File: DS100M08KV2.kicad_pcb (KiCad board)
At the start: 4 copper layers, 100 x 52 mm, 129 parts, among them J1 wire2board, J10 BNC_panel_mount, J11 wire2board, J2 Conn_01x04_Socket, J3 wire2board, J4 wire2board, J5 USB_C_floating, J8 red_safety_4mm_connector, J9 black_safety_4mm_connector, Q1 BD679, Q3 CMSN3416K-HF, Q4 BD680, Q5 CMSN3416K-HF, SW1 SW_DPDT_x2, SW2 SW_DPDT_x2, U1 AD8066, U2 AP9101CK6, U4 AD8009, U6 BQ21040DBV, U7 TLV61070ADBVR

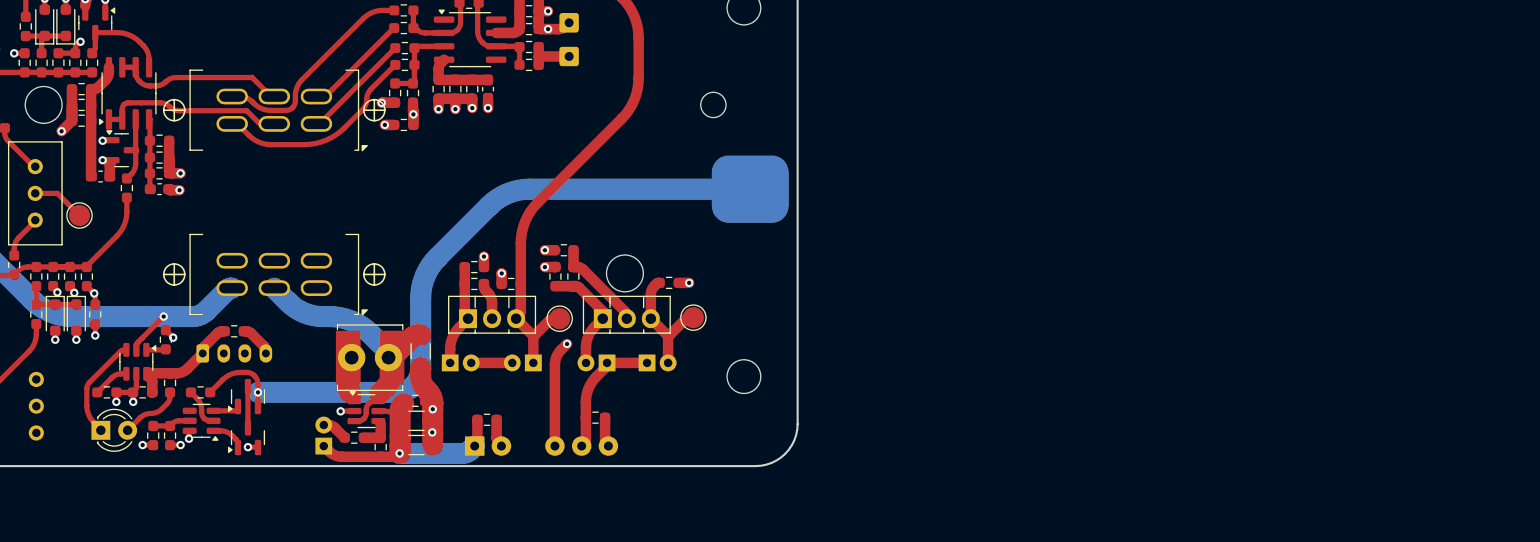
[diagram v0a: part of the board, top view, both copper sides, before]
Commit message: New sims, added switcher to PCB.
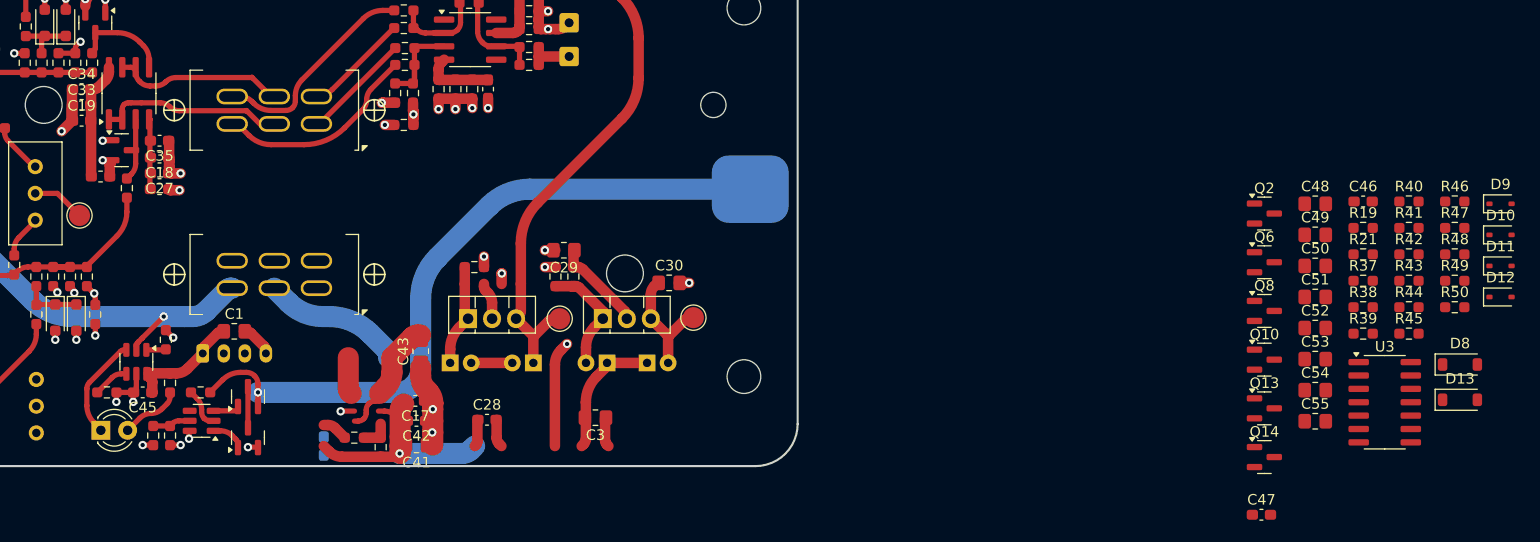
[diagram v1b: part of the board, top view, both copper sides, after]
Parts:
- removed C31: 1u, Resistor_SMD:R_0603_1608Metric_Pad0.98x0.95mm_HandSolder
- removed L2: 4.7u, Inductor_THT:L_Radial_D7.5mm_P3.50mm_Fastron_07P
- removed L3: 4.7u, Inductor_SMD:L_Bourns_SRN6045TA
- removed PS1: IA0509S, Converter_DCDC:Converter_DCDC_XP_POWER-IAxxxxS_THT
- removed R31: 1k, Resistor_SMD:R_0603_1608Metric_Pad0.98x0.95mm_HandSolder
- removed U7: TLV61070ADBVR, Package_TO_SOT_SMD:SOT-23-6
- added C46: 1u, Capacitor_SMD:C_0603_1608Metric_Pad1.08x0.95mm_HandSolder, F.Cu at (253.7, 126.9)
- added C47: 100n, Capacitor_SMD:C_0603_1608Metric_Pad1.08x0.95mm_HandSolder, F.Cu at (244.0, 156.6)
- added C48: 10u, Resistor_SMD:R_0805_2012Metric_Pad1.20x1.40mm_HandSolder, F.Cu at (249.2, 127.1)
- added C49: 10u, Resistor_SMD:R_0805_2012Metric_Pad1.20x1.40mm_HandSolder, F.Cu at (249.2, 130.0)
- added C50: 10u, Resistor_SMD:R_0805_2012Metric_Pad1.20x1.40mm_HandSolder, F.Cu at (249.2, 133.0)
- added C51: 10u, Resistor_SMD:R_0805_2012Metric_Pad1.20x1.40mm_HandSolder, F.Cu at (249.2, 135.9)
- added C52: 10u, Resistor_SMD:R_0805_2012Metric_Pad1.20x1.40mm_HandSolder, F.Cu at (249.2, 138.9)
- added C53: 10u, Resistor_SMD:R_0805_2012Metric_Pad1.20x1.40mm_HandSolder, F.Cu at (249.2, 141.8)
- added C54: 10u, Resistor_SMD:R_0805_2012Metric_Pad1.20x1.40mm_HandSolder, F.Cu at (249.2, 144.8)
- added C55: 10u, Resistor_SMD:R_0805_2012Metric_Pad1.20x1.40mm_HandSolder, F.Cu at (249.2, 147.7)
- added D10: 1N4148WS, Diode_SMD:D_SOD-323, F.Cu at (266.8, 130.0)
- added D11: 1N4148WS, Diode_SMD:D_SOD-323, F.Cu at (266.8, 133.0)
- added D12: 1N4148WS, Diode_SMD:D_SOD-323, F.Cu at (266.8, 135.9)
- added D13: 1N4148W, Diode_SMD:D_SOD-123, F.Cu at (262.9, 145.7)
- added D8: 1N4148W, Diode_SMD:D_SOD-123, F.Cu at (262.9, 142.3)
- added D9: 1N4148WS, Diode_SMD:D_SOD-323, F.Cu at (266.8, 127.1)
- added Q10: AO3401A, Package_TO_SOT_SMD:SOT-23, F.Cu at (244.3, 141.9)
- added Q13: AO3400A, Package_TO_SOT_SMD:SOT-23, F.Cu at (244.3, 146.5)
- added Q14: AO3400A, Package_TO_SOT_SMD:SOT-23, F.Cu at (244.3, 151.1)
- added Q2: MMBT5551L, Package_TO_SOT_SMD:SOT-23, F.Cu at (244.3, 128.0)
- added Q6: MMBT5551L, Package_TO_SOT_SMD:SOT-23, F.Cu at (244.3, 132.6)
- added Q8: AO3401A, Package_TO_SOT_SMD:SOT-23, F.Cu at (244.3, 137.3)
- added R19: 39k, Resistor_SMD:R_0603_1608Metric_Pad0.98x0.95mm_HandSolder, F.Cu at (253.7, 129.4)
- added R21: 470k, Resistor_SMD:R_0603_1608Metric_Pad0.98x0.95mm_HandSolder, F.Cu at (253.7, 131.9)
- added R37: 100k, Resistor_SMD:R_0603_1608Metric_Pad0.98x0.95mm_HandSolder, F.Cu at (253.7, 134.4)
- added R38: 100k, Resistor_SMD:R_0603_1608Metric_Pad0.98x0.95mm_HandSolder, F.Cu at (253.7, 136.9)
- added R39: 470k, Resistor_SMD:R_0603_1608Metric_Pad0.98x0.95mm_HandSolder, F.Cu at (253.7, 139.4)
- added R40: 10k, Resistor_SMD:R_0603_1608Metric_Pad0.98x0.95mm_HandSolder, F.Cu at (258.1, 126.9)
- added R41: 470k, Resistor_SMD:R_0603_1608Metric_Pad0.98x0.95mm_HandSolder, F.Cu at (258.1, 129.4)
- added R42: 1k, Resistor_SMD:R_0603_1608Metric_Pad0.98x0.95mm_HandSolder, F.Cu at (258.1, 131.9)
- added R43: 470k, Resistor_SMD:R_0603_1608Metric_Pad0.98x0.95mm_HandSolder, F.Cu at (258.1, 134.4)
- added R44: 470k, Resistor_SMD:R_0603_1608Metric_Pad0.98x0.95mm_HandSolder, F.Cu at (258.1, 136.9)
- added R45: 1Meg, Resistor_SMD:R_0603_1608Metric_Pad0.98x0.95mm_HandSolder, F.Cu at (258.1, 139.4)
- added R46: 1Meg, Resistor_SMD:R_0603_1608Metric_Pad0.98x0.95mm_HandSolder, F.Cu at (262.4, 126.9)
- added R47: 470k, Resistor_SMD:R_0603_1608Metric_Pad0.98x0.95mm_HandSolder, F.Cu at (262.4, 129.4)
- added R48: 1Meg, Resistor_SMD:R_0603_1608Metric_Pad0.98x0.95mm_HandSolder, F.Cu at (262.4, 131.9)
- added R49: 1Meg, Resistor_SMD:R_0603_1608Metric_Pad0.98x0.95mm_HandSolder, F.Cu at (262.4, 134.4)
- added R50: 1k, Resistor_SMD:R_0603_1608Metric_Pad0.98x0.95mm_HandSolder, F.Cu at (262.4, 136.9)
- added U3: 74HC14D653, Package_SO:SOIC-14_3.9x8.7mm_P1.27mm, F.Cu at (255.8, 145.9)
- C1, C29, C3, C30: value 1u -> 10u; footprint Resistor_SMD:R_0603_1608Metric_Pad0.98x0.95mm_HandSolder -> Resistor_SMD:R_0805_2012Metric_Pad1.20x1.40mm_HandSolder
- C17: value 1u -> 1n; footprint Resistor_SMD:R_0603_1608Metric_Pad0.98x0.95mm_HandSolder -> Capacitor_SMD:C_0603_1608Metric_Pad1.08x0.95mm_HandSolder
- C18: value 100n -> 10u; footprint Resistor_SMD:R_0603_1608Metric_Pad0.98x0.95mm_HandSolder -> Capacitor_SMD:C_0603_1608Metric_Pad1.08x0.95mm_HandSolder
- C19: value 1u -> 10u; footprint Resistor_SMD:R_0603_1608Metric_Pad0.98x0.95mm_HandSolder -> Capacitor_SMD:C_0603_1608Metric_Pad1.08x0.95mm_HandSolder
- C23, C24: value 470p -> 1n
- C27, C28: value 1u -> 100n; footprint Resistor_SMD:R_0603_1608Metric_Pad0.98x0.95mm_HandSolder -> Capacitor_SMD:C_0603_1608Metric_Pad1.08x0.95mm_HandSolder
- C33: value 100n -> 100p; footprint Resistor_SMD:R_0603_1608Metric_Pad0.98x0.95mm_HandSolder -> Capacitor_SMD:C_0603_1608Metric_Pad1.08x0.95mm_HandSolder
- C34: value 1n -> 100p; footprint Resistor_SMD:R_0603_1608Metric_Pad0.98x0.95mm_HandSolder -> Capacitor_SMD:C_0603_1608Metric_Pad1.08x0.95mm_HandSolder
- C35: value 1n -> 100n; footprint Resistor_SMD:R_0603_1608Metric_Pad0.98x0.95mm_HandSolder -> Capacitor_SMD:C_0603_1608Metric_Pad1.08x0.95mm_HandSolder
- C40: value 47u -> 1u; footprint Capacitor_THT:CP_Radial_D5.0mm_P2.00mm -> Capacitor_SMD:C_0603_1608Metric_Pad1.08x0.95mm_HandSolder
- C41, C43: footprint Resistor_SMD:R_1206_3216Metric_Pad1.30x1.75mm_HandSolder -> Resistor_SMD:R_0805_2012Metric_Pad1.20x1.40mm_HandSolder
- C42: value 10u -> 100n; footprint Resistor_SMD:R_1206_3216Metric_Pad1.30x1.75mm_HandSolder -> Capacitor_SMD:C_0603_1608Metric_Pad1.08x0.95mm_HandSolder
- C45: footprint Resistor_SMD:R_0603_1608Metric_Pad0.98x0.95mm_HandSolder -> Capacitor_SMD:C_0603_1608Metric_Pad1.08x0.95mm_HandSolder
- Q1: value BD679 -> MMBT5401
- Q4: value BD680 -> MMBT5401
- R12, R5: value 10k -> 5k
- R27: value 10k -> 22k
- R28: value 91k -> 100k
- R32: value 2k2 -> 22k
- R34: value 2k2 -> 100k
- U1: value AD8066 -> RS8752XK
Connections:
- BT1 pad 1: +BAT -> +BATT
- BT1 pad 2: -BAT -> -BATT
- C1 pad 1: +VBUS -> -BATT
- C1 pad 2: Earth -> -VIN
- C16 pad 1: Net-(Q1-B) -> Net-(Q2-B)
- C17 pad 1: Earth -> -BATT
- C17 pad 2: +5V_BOOST -> Net-(C17-Pad2)
- C18 pad 1: 0 -> Net-(U1C-V-)
- C18 pad 2: Net-(U1C-V-) -> 0
- C19 pad 1: 0 -> Net-(U1C-V+)
- C19 pad 2: Net-(U1C-V+) -> 0
- C20 pad 2: Net-(Q4-B) -> Net-(Q1-B)
- C27 pad 1: 0 -> PMOS_GATE
- C27 pad 2: Net-(U1C-V-) -> Net-(D8-A)
- C28 pad 1: +5V_BOOST -> Earth
- C28 pad 2: Earth -> +VBUS
- C29 pad 1: Net-(PS1--Vout) -> 0
- C29 pad 2: 0 -> +2V5
- C3 pad 1: Net-(PS1-+Vout) -> -VIN
- C30 pad 1: -5V -> -2V5
- C33 pad 1: 0 -> -BATT
- C33 pad 2: Net-(U1C-V+) -> Net-(D11-K)
- C34 pad 1: 0 -> -BATT
- C34 pad 2: Net-(U1C-V+) -> Net-(D12-A)
- C36 pad 2: -5V -> -2V5
- C40 pad 1: +5V_BOOST -> Earth
- C40 pad 2: Earth -> +VBUS
- C41 pad 1: Earth -> Net-(Q13-D)
- C41 pad 2: +5V_BOOST -> Net-(Q10-D)
- C42 pad 1: Earth -> NMOS_GATE
- C42 pad 2: +5V_BOOST -> Net-(D13-A)
- C43 pad 1: Earth -> Net-(Q13-D)
- C43 pad 2: Net-(SW2A-B) -> Net-(Q10-D)
- C44 pad 1: +5V -> +2V5
- C45 pad 1: +VBUS -> -BATT
- C45 pad 2: Earth -> +VIN
- Q1 pad 2: Net-(PS1-+Vout) -> -2V5
- Q1 pad 3: +5V -> -VIN
- Q4 pad 2: Net-(PS1--Vout) -> 0
- Q4 pad 3: -5V -> Net-(Q1-B)
- R27 pad 1: Earth -> Net-(Q6-B)
- R27 pad 2: Net-(U7-FB) -> 0
- R28 pad 1: Net-(U7-FB) -> Net-(Q1-B)
- R28 pad 2: +5V_BOOST -> Net-(Q4-B)
- R32 pad 1: 0 -> Net-(Q4-B)
- R32 pad 2: Net-(Q1-B) -> 0
- R33 pad 1: Net-(Q4-B) -> Net-(Q2-B)
- R33 pad 2: Net-(PS1--Vout) -> +VIN
- R34 pad 1: 0 -> Net-(Q6-B)
- R34 pad 2: Net-(Q4-B) -> Net-(Q2-B)
- SW2 pad 2: Net-(SW2A-B) -> +VIN
- SW2 pad 3: +BAT -> +BATT
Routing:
- net Net-(PS1-+Vout): track 24.7 -> 0.00 mm
- net Net-(SW2A-B): track 24.2 -> 0.00 mm
- net -2V5: track 0.00 -> 21.9 mm
- net +VIN: track 0.00 -> 13.4 mm, vias 0 -> 1
- net Net-(Q10-D): track 0.00 -> 10.8 mm
- net (no net): track 0.00 -> 6.38 mm
- net Net-(U7-SW): track 3.49 -> 0.00 mm
- net Net-(Q6-B): track 0.00 -> 3.44 mm, vias 0 -> 1
- net 0: track 67.2 -> 64.2 mm, vias 24 -> 21
- net Net-(U7-FB): track 2.89 -> 0.00 mm
- net -VIN: track 0.00 -> 2.80 mm
- net +VBUS: track 10.9 -> 13.6 mm
- net +5V_BOOST: track 24.8 -> 22.2 mm, vias 1 -> 0
- net Earth: track 26.3 -> 23.8 mm
- net Net-(Q4-B): track 11.5 -> 12.5 mm, vias 0 -> 2
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
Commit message: Sims, schem.
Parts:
- removed FB3, FB4: FerriteBead, Inductor_SMD:L_0603_1608Metric_Pad1.05x0.95mm_HandSolder
- removed RV4: 100k, Potentiometer_THT:Potentiometer_Bourns_3296W_Vertical
- removed U4: AD8009, Package_SO:SOIC-8_3.9x4.9mm_P1.27mm
- added C56: 100p, Resistor_SMD:R_0603_1608Metric_Pad0.98x0.95mm_HandSolder, F.Cu at (233.5, 135.5)
- added C57: 10p, Resistor_SMD:R_0603_1608Metric_Pad0.98x0.95mm_HandSolder, F.Cu at (233.5, 138.0)
- added C58: 10p, Resistor_SMD:R_0603_1608Metric_Pad0.98x0.95mm_HandSolder, F.Cu at (233.5, 140.5)
- added R31: 100, Resistor_SMD:R_0603_1608Metric_Pad0.98x0.95mm_HandSolder, F.Cu at (150.6, 112.6)
- added R53: 200, Resistor_SMD:R_0603_1608Metric_Pad0.98x0.95mm_HandSolder, F.Cu at (233.5, 143.0)
- added R54: 100, Resistor_SMD:R_0603_1608Metric_Pad0.98x0.95mm_HandSolder, F.Cu at (150.6, 115.1)
- C21, C22, C4: value 100n -> 330p
- C23, C24, C25, C37: value 1n -> 100p
- C26: value 1u -> 100p
- C32, C7, C8: footprint Resistor_SMD:R_0603_1608Metric_Pad0.98x0.95mm_HandSolder -> Capacitor_SMD:C_0603_1608Metric_Pad1.08x0.95mm_HandSolder
- C38: value 100n -> 100p
- C5: value 470p -> 330p
- C6: value 470p -> 100p
- R12, R5: value 5k -> 10k
- R13: value 50 -> 82k
- R16: value 10 -> 10k
- R18: value 1k -> 82k
- R20: value 100 -> 200
- R24: value 51k -> 200
- R6: value 500 -> 10k
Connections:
- C21 pad 1: 0 -> Net-(C21-Pad1)
- C21 pad 2: Net-(U4-V+) -> 0
- C22 pad 1: 0 -> Net-(C21-Pad1)
- C22 pad 2: Net-(U4-V-) -> 0
- C23 pad 2: Net-(C15-Pad1) -> Net-(C21-Pad1)
- C24 pad 2: Net-(C11-Pad1) -> Net-(C21-Pad1)
- C25 pad 1: 0 -> Net-(C21-Pad1)
- C25 pad 2: Net-(U4-V-) -> Net-(C11-Pad1)
- C26 pad 2: Net-(U4-V+) -> Net-(C26-Pad2)
- C37 pad 2: Net-(U4-V+) -> Net-(C26-Pad2)
- C38 pad 2: Net-(U4-V-) -> Net-(C26-Pad2)
- C4 pad 1: 0 -> Net-(C26-Pad2)
- C4 pad 2: Net-(C4-Pad2) -> 0
- C5 pad 1: 0 -> Net-(C26-Pad2)
- C5 pad 2: Net-(C15-Pad1) -> 0
- C6 pad 2: Net-(C11-Pad1) -> Net-(C21-Pad1)
- C7 pad 2: Net-(C11-Pad1) -> Net-(C21-Pad1)
- C8 pad 1: Net-(D4-K) -> Net-(C26-Pad2)
- C8 pad 2: Net-(C15-Pad1) -> Net-(D4-K)
- D2 pad 3: Net-(U1B-+) -> Net-(SW1B-B)
- D7 pad 3: Net-(U1A-+) -> Net-(SW1A-B)
- R12 pad 2: Net-(C15-Pad1) -> Net-(C26-Pad2)
- R13 pad 1: Net-(U4--) -> Net-(C21-Pad1)
- R13 pad 2: Net-(SW1B-C) -> Net-(R13-Pad2)
- R16 pad 1: Net-(SW1A-A) -> Net-(R16-Pad1)
- R16 pad 2: Net-(U4-+) -> Net-(C26-Pad2)
- R18 pad 1: Net-(U4--) -> Net-(C15-Pad1)
- R18 pad 2: Net-(R17-Pad2) -> Net-(R16-Pad1)
- R20 pad 1: Net-(SW1A-C) -> Net-(U1A--)
- R20 pad 2: Net-(U4-+) -> Net-(R17-Pad2)
- R22 pad 1: Net-(U4-+) -> Net-(R22-Pad1)
- R22 pad 2: 0 -> Net-(U1A--)
- R24 pad 1: Net-(C4-Pad2) -> Net-(U1B--)
- R24 pad 2: Net-(U4-+) -> 0
- R5 pad 2: Net-(C11-Pad1) -> Net-(C21-Pad1)
- R51 pad 1: Net-(U1A-+) -> Net-(SW1B-A)
- R51 pad 2: Net-(C11-Pad1) -> Net-(C26-Pad2)
- R52 pad 1: Net-(U1B-+) -> Net-(C15-Pad1)
- R52 pad 2: Net-(C15-Pad1) -> Net-(SW1B-C)
- R6 pad 1: Net-(U4--) -> Net-(R13-Pad2)
- R6 pad 2: Net-(SW1B-A) -> Net-(C11-Pad1)
- U1 pad 1: Net-(SW1A-B) -> Net-(R17-Pad2)
- U1 pad 2: Net-(SW1A-B) -> Net-(U1A--)
- U1 pad 3: Net-(U1A-+) -> Net-(SW1A-B)
- U1 pad 5: Net-(U1B-+) -> Net-(SW1B-B)
- U1 pad 6: Net-(SW1B-B) -> Net-(U1B--)
- U1 pad 7: Net-(SW1B-B) -> Net-(R22-Pad1)
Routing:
- net (no net): track 6.38 -> 111.2 mm
- net Net-(PS1--Vout): track 26.4 -> 0.00 mm
- net +5V_BOOST: track 22.2 -> 0.00 mm
- net Net-(C4-Pad2): track 16.4 -> 0.00 mm, vias 1 -> 0
- net Net-(U4-+): track 9.55 -> 0.00 mm
- net Net-(U1B-+): track 9.17 -> 0.00 mm
- net Net-(U4--): track 8.47 -> 0.00 mm
- net Net-(U4-V+): track 7.32 -> 0.00 mm
- net Net-(U4-V-): track 6.77 -> 0.00 mm
- net Net-(U1A-+): track 5.90 -> 0.00 mm
- net 0: track 64.2 -> 69.4 mm, vias 21 -> 19
- net Net-(U1A--): track 0.00 -> 1.28 mm, vias 0 -> 1
- net Net-(C26-Pad2): track 0.00 -> 0.89 mm, vias 0 -> 1
- net Net-(U1B--): vias 0 -> 1

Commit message: Layout.
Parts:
- Q1, Q4: footprint Package_TO_SOT_THT:TO-126-3_Vertical -> Package_TO_SOT_SMD:SOT-23
- moved C56 107.9 mm to (126.9, 119.0), turned to -90 degrees
- moved C58 107.1 mm to (128.6, 119.0), turned to -90 degrees
- moved C57 105.2 mm to (128.4, 132.7), turned to -90 degrees
- moved C25 45.4 mm to (126.8, 132.7), turned to -90 degrees
- moved R6 45.4 mm to (125.2, 134.4), turned to -90 degrees
- moved R18 44.6 mm to (125.2, 117.3), turned to -90 degrees
- moved R13 42.7 mm to (125.2, 131.1), turned to -90 degrees
- moved R16 38.4 mm to (125.2, 120.6), turned to -90 degrees
- moved SW2 28.0 mm to (177.2, 126.0)
- moved C19 20.0 mm to (151.2, 124.7)
- moved C33 20.0 mm to (151.2, 123.2)
- moved C34 20.0 mm to (151.2, 121.7)
- moved C35 20.0 mm to (158.6, 126.6)
- moved D7 20.0 mm to (155.0, 127.5)
- moved FB2 20.0 mm to (153.0, 130.0)
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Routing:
- net +5V: track 181.8 -> 11.5 mm, vias 2 -> 1
- net -5V: track 146.0 -> 0.00 mm, vias 4 -> 2
- net (no net): track 111.2 -> 0.00 mm
- net 0: track 69.4 -> 0.98 mm, vias 19 -> 15
- net -BAT: track 67.8 -> 0.00 mm
- net +BAT: track 53.5 -> 0.00 mm
- net Earth: track 23.8 -> 0.00 mm
- net -2V5: track 21.9 -> 0.00 mm
- net Net-(SW1B-A): track 20.5 -> 0.00 mm
- net Net-(SW1A-C): track 18.8 -> 0.00 mm
- net Net-(C11-Pad1): track 24.4 -> 6.96 mm
- net Net-(SW1A-B): track 17.1 -> 0.00 mm
- net Net-(SW1B-B): track 15.4 -> 0.00 mm
- net Net-(C32-Pad2): track 14.6 -> 0.00 mm, vias 1 -> 0
- net +VBUS: track 13.6 -> 0.00 mm
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- removed copper zone on In1.Cu, net 0
- removed copper zone on In1.Cu, net Earth

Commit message: Layout
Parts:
- added C31: 100n, Capacitor_SMD:C_0603_1608Metric_Pad1.08x0.95mm_HandSolder, F.Cu at (166.0, 144.5)
- added C59: 100n, Capacitor_SMD:C_0603_1608Metric_Pad1.08x0.95mm_HandSolder, F.Cu at (176.7, 140.1)
- added C60: 100n, Capacitor_SMD:C_0603_1608Metric_Pad1.08x0.95mm_HandSolder, F.Cu at (172.6, 144.3)
- added C61: 47u, Capacitor_THT:CP_Radial_D5.0mm_P2.00mm, B.Cu at (169.8, 148.8)
- added C62: 47u, Capacitor_THT:CP_Radial_D5.0mm_P2.00mm, B.Cu at (169.8, 139.9)
- added C63: 47u, Capacitor_THT:CP_Radial_D5.0mm_P2.00mm, B.Cu at (186.0, 140.7)
- added C64: 47u, Capacitor_THT:CP_Radial_D5.0mm_P2.00mm, B.Cu at (186.0, 144.2)
- added C65: 10u, Resistor_SMD:R_0805_2012Metric_Pad1.20x1.40mm_HandSolder, F.Cu at (172.6, 138.8)
- C40: moved to F.Cu
- moved R28 170.1 mm to (327.4, 118.0), turned to 180 degrees
- moved C16 163.2 mm to (324.6, 99.7), turned to -90 degrees
- moved R27 158.1 mm to (309.1, 102.9)
- moved Q1 156.7 mm to (324.8, 124.3), turned to -90 degrees
- moved R34 153.7 mm to (327.6, 103.3), turned to 180 degrees
- moved C44 148.2 mm to (317.0, 99.9), turned to -90 degrees
- moved C20 146.8 mm to (327.5, 123.4), turned to -90 degrees
- moved Q4 146.7 mm to (327.2, 120.5)
- moved R32 145.7 mm to (314.6, 122.3)
- moved C29 144.5 mm to (319.0, 100.8), turned to 90 degrees
- moved R33 143.5 mm to (319.8, 107.8)
- moved C3 137.8 mm to (314.1, 112.4)
- moved C30 134.7 mm to (322.1, 124.1), turned to -90 degrees
- moved C36 134.5 mm to (319.2, 125.9), turned to 90 degrees
- moved D9 120.7 mm to (147.6, 146.5), turned to 90 degrees
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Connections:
- net Net-(Q10-D) renamed /Power supply/MID_REC
- net Net-(Q13-D) renamed /Power supply/MID_DRV
- C17 pad 2: Net-(C17-Pad2) -> Net-(D10-A)
- D10 pad 1: CLK -> Net-(D10-K)
- R19 pad 2: Net-(C17-Pad2) -> Net-(D10-A)
- R21 pad 1: Net-(C17-Pad2) -> Net-(D10-A)
- R37 pad 1: Net-(C17-Pad2) -> Net-(D10-A)
- R38 pad 1: Net-(C17-Pad2) -> Net-(D10-K)
- R38 pad 2: Net-(D10-A) -> CLK
- R39 pad 1: Net-(C17-Pad2) -> Net-(D10-K)
- R39 pad 2: Net-(D10-A) -> CLK
- U3 pad 1: Net-(C17-Pad2) -> Net-(D12-A)
- U3 pad 2: CLK -> PMOS_GATE
- U3 pad 8: PMOS_GATE -> CLK
- U3 pad 9: Net-(D12-A) -> Net-(D10-A)
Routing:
- net +5V: track 11.5 -> 0.00 mm, vias 1 -> 0
- net Net-(R15-Pad2): track 7.40 -> 0.00 mm
- net Net-(C15-Pad1): track 9.21 -> 4.70 mm
- net +BATT: track 3.63 -> 0.00 mm
- net Net-(R14-Pad2): track 1.68 -> 0.00 mm
- net Net-(C11-Pad1): vias 0 -> 1
- net Earth: vias 9 -> 6
- net 0: vias 15 -> 12
- net /Power supply/MID_REC: vias 1 -> 0
- net -BATT: vias 0 -> 2
- net -5V: vias 2 -> 1
- net +VIN: vias 1 -> 0

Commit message: Placement done.
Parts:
- removed H2: MountingHole, DS100M08KV:M3_with_screw
- added C66: 100n, Capacitor_SMD:C_0603_1608Metric_Pad1.08x0.95mm_HandSolder, F.Cu at (139.1, 107.2)
- added C67: 100n, Capacitor_SMD:C_0603_1608Metric_Pad1.08x0.95mm_HandSolder, F.Cu at (119.7, 148.3)
- added R55: 1k, Resistor_SMD:R_0603_1608Metric_Pad0.98x0.95mm_HandSolder, F.Cu at (186.7, 101.0)
- added R56: 10k, Resistor_SMD:R_0603_1608Metric_Pad0.98x0.95mm_HandSolder, F.Cu at (193.2, 102.6)
- added TP6: TestPoint, TestPoint:TestPoint_Pad_D2.0mm, F.Cu at (167.1, 107.5)
- added TP7: TestPoint, TestPoint:TestPoint_Pad_D2.0mm, F.Cu at (189.4, 149.7)
- added TP8: TestPoint, TestPoint:TestPoint_Pad_D2.0mm, F.Cu at (189.3, 144.1)
- added TP9: TestPoint, TestPoint:TestPoint_Pad_D2.0mm, F.Cu at (189.4, 139.3)
- added U4: TL431DBZ, Package_TO_SOT_SMD:SOT-23, F.Cu at (190.4, 102.3)
- moved R50 161.5 mm to (175.4, 109.0)
- moved C30 148.8 mm to (173.8, 111.9), turned to 90 degrees
- moved Q1 148.7 mm to (176.6, 111.8)
- moved C20 148.7 mm to (179.3, 110.9)
- moved C36 148.1 mm to (171.8, 111.0), turned to -90 degrees
- moved C16 145.2 mm to (179.4, 102.1)
- moved Q2 145.2 mm to (176.6, 103.0)
- moved R34 145.2 mm to (182.4, 105.6)
- moved C29 145.2 mm to (173.8, 103.1)
- moved C44 145.2 mm to (171.8, 102.3)
- moved Q6 145.2 mm to (182.5, 103.1)
- moved Q4 145.2 mm to (182.3, 111.8)
- moved R28 145.2 mm to (182.5, 109.3)
- moved C55 144.8 mm to (175.4, 106.1), turned to 0 degrees
- moved C3 142.3 mm to (171.8, 108.8)
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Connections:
- D2 pad 1: -5V -> -2V5
- D2 pad 2: +5V -> +2V5
- D7 pad 1: -5V -> -2V5
- D7 pad 2: +5V -> +2V5
- FB1 pad 2: -5V -> -2V5
- FB2 pad 2: +5V -> +2V5
- R20 pad 1: Net-(U1A--) -> Net-(U1B--)
- R22 pad 2: Net-(U1A--) -> Net-(U1B--)
- R24 pad 1: Net-(U1B--) -> Net-(U1A--)
- R31 pad 1: Net-(SW1A-A) -> Net-(SW1A-C)
- R51 pad 1: Net-(SW1B-A) -> Net-(SW1B-C)
- R52 pad 2: Net-(SW1B-C) -> Net-(SW1B-A)
- R53 pad 2: Net-(U1B--) -> Net-(U1A--)
- R54 pad 2: Net-(SW1A-C) -> Net-(SW1A-A)
- RV1 pad 1: -5V -> -2V5
- RV1 pad 3: +5V -> +2V5
- RV5 pad 3: +5V -> +2V5
- RV6 pad 3: +5V -> unconnected-(RV6-Pad3)
- TP3 pad 1: +5V -> +2V5
- TP4 pad 1: -5V -> -2V5
- U1 pad 1: Net-(R17-Pad2) -> Net-(R22-Pad1)
- U1 pad 3: Net-(SW1A-B) -> Net-(SW1B-B)
- U1 pad 5: Net-(SW1B-B) -> Net-(SW1A-B)
- U1 pad 7: Net-(R22-Pad1) -> Net-(R17-Pad2)
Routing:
- net Net-(SW1B-B): track 0.00 -> 18.1 mm
- net Net-(SW1A-B): track 0.00 -> 9.99 mm
- net Net-(C15-Pad1): track 4.70 -> 3.46 mm
- net 0: track 0.98 -> 0.00 mm, vias 12 -> 0
- net Net-(C11-Pad1): track 6.96 -> 7.88 mm
- net Net-(U1B--): vias 1 -> 0
- net Net-(U1A--): vias 1 -> 0
- net Net-(SW1A-C): vias 0 -> 1
- net Net-(Q6-B): vias 1 -> 0
- net Net-(Q4-B): vias 1 -> 0
- net Net-(C26-Pad2): vias 1 -> 0
- net Earth: vias 6 -> 5
- net -5V: vias 1 -> 0
- net +2V5: vias 1 -> 0
- added copper zone on B.Cu, net -VIN
- added copper zone on B.Cu, net 0

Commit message: Switcher done.
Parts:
- moved TP5 17.6 mm to (134.9, 126.0)
- moved C27 3.68 mm to (176.7, 148.5), turned to 0 degrees
- moved D8 2.97 mm to (180.8, 147.6)
- moved TP2 0.85 mm to (125.9, 139.4)
- moved R26 0.30 mm to (134.1, 144.5)
- moved C32 0.22 mm to (125.2, 110.0)
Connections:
- Q5 pad 2: -BAT -> -BATT
- R29 pad 1: -BAT -> -BATT
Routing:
- net +VIN: track 0.00 -> 62.1 mm, vias 0 -> 1
- net -BATT: track 0.00 -> 37.3 mm, vias 2 -> 11
- net NMOS_GATE: track 0.00 -> 31.8 mm, vias 0 -> 3
- net 0: track 0.00 -> 29.3 mm, vias 0 -> 14
- net PMOS_GATE: track 0.00 -> 27.8 mm, vias 0 -> 2
- net -VIN: track 0.00 -> 27.7 mm, vias 0 -> 2
- net Net-(D12-A): track 0.00 -> 24.8 mm
- net CLK: track 0.00 -> 23.6 mm, vias 0 -> 2
- net Net-(SW1B-A): track 0.00 -> 22.6 mm
- net Net-(SW1A-C): track 0.00 -> 22.3 mm
- net Net-(C67-Pad2): track 0.00 -> 22.2 mm, vias 0 -> 2
- net +BAT: track 0.00 -> 19.1 mm
- net /Power supply/MID_REC: track 0.00 -> 16.7 mm
- net Net-(C26-Pad2): track 0.00 -> 15.4 mm
- net Net-(C21-Pad1): track 0.00 -> 15.3 mm
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- added copper zone on B.Cu, net -BATT
- added copper zone on F.Cu, net -BATT
- added copper zone on F.Cu, net /Power supply/MID_DRV
- added copper zone on F.Cu, net /Power supply/MID_REC
- removed copper zone on B.Cu, net -VIN

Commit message: Lin Reg.
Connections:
- SW2 pad 4: unconnected-(SW2B-A-Pad4) -> +BATT
- SW2 pad 5: unconnected-(SW2B-B-Pad5) -> +VIN
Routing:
- net -VIN: track 27.7 -> 72.9 mm, vias 2 -> 6
- net +VIN: track 62.1 -> 87.6 mm, vias 1 -> 2
- net Net-(Q2-B): track 0.00 -> 25.4 mm, vias 0 -> 2
- net Net-(Q1-B): track 0.00 -> 21.3 mm
- net Net-(Q4-B): track 0.00 -> 20.8 mm, vias 0 -> 2
- net +2V5: track 0.00 -> 14.9 mm
- net 0: track 29.3 -> 44.1 mm, vias 14 -> 23
- net Net-(Q6-B): track 0.00 -> 14.0 mm
- net -2V5: track 0.00 -> 9.57 mm
- net Net-(U4-REF): track 0.00 -> 7.04 mm, vias 0 -> 2
- net +BATT: track 0.00 -> 2.60 mm
